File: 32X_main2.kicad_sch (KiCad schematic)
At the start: 54 parts, among them IC501 SH2 M, IC502 SH2 S, IC503 µPD4502161, IC504 315-5818, IC506 315-5781, IC507 TC511664, IC508 TC511664, IC509 74AC04, IC510 RHSRL33A

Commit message: more component parts updated
Full in the * as PAL versions.
Added MPN for PCBWAY
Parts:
- C5, C513, C516, C518, C519, C521, C522, C528, C531, C532, C533, C535, C536, C538, C539, C540, C541, C548: MPN (none) -> VJ0805Y104JXJMT
- C511, C514: MPN (none) -> VJ0805A471FXJPW1BC
- C512, C515, C517, C520, C523, C527, C530, C534, C537, C699: MPN (none) -> VJ1206V475MXJTW1BC
- C525: MPN (none) -> VJ0805A680FXJCW1BC
- C526, C696, C697: MPN (none) -> VJ0805A101FXJPW1BC
- IC509: MPN (none) -> SN74AC04DR
- L501: MPN (none) -> CMI322513J101KT
- R502: MPN (none) -> CRCW080510K0FKEA
- R503, R505: MPN (none) -> CRCW08053K00FKEA
- R506: MPN (none) -> CRCW0805180RJNEA
- R507: MPN (none) -> CRCW080513K0FKEA
- R508: MPN (none) -> CRCW08052K70FKEA
- R509: MPN (none) -> CRCW08051K60FKEA

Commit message: part updates
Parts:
- C525: LCSC Part # C3842272 -> C162306; MPN VJ0805A680FXJCW1BC -> GRM21A5C2J680JWA1D
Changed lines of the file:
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@@
       (effects (font (size 1.27 1.27)) hide)
     )
-    (property "LCSC Part #" "C3842272" (at 215.265 203.835 0)
+    (property "LCSC Part #" "C162306" (at 215.265 203.835 0)
       (effects (font (size 1.27 1.27)) hide)
     )
-    (property "MPN" "VJ0805A680FXJCW1BC" (at 215.265 203.835 0)
+    (property "MPN" "GRM21A5C2J680JWA1D" (at 215.265 203.835 0)
       (effects (font (size 1.27 1.27)) hide)
     )

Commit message: Allow for both wide and narrow IC509.
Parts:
- IC509: footprint Package_SO:SO-14_5.3x10.2mm_P1.27mm -> Neptune:SO-14_Dual_Purpose_P1.27mm
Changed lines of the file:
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@@
       (effects (font (size 1.27 1.27)))
     )
-    (property "Footprint" "Package_SO:SO-14_5.3x10.2mm_P1.27mm" (at 377.19 232.41 0)
+    (property "Footprint" "Neptune:SO-14_Dual_Purpose_P1.27mm" (at 377.19 232.41 0)
       (effects (font (size 1.27 1.27)) hide)
     )
@@
       (effects (font (size 1.27 1.27)))
     )
-    (property "Footprint" "Package_SO:SO-14_5.3x10.2mm_P1.27mm" (at 340.995 232.41 0)
-      (effects (font (size 1.27 1.27)) hide)
-    )
+    (property "Footprint" "Neptune:SO-14_Dual_Purpose_P1.27mm" (at 340.995 232.41 0)
+      (effects (font (size 1.27 1.27)) hide)
+    )

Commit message: Update LCSC parts
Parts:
- C5, C513, C516, C518, C519, C521, C522, C528, C531, C532, C533, C535, C536, C538, C539, C540, C541, C548: LCSC Part # C2237864 -> C111492
- C511, C514: LCSC Part # C2232577 -> C62771
- C512, C515, C517, C520, C523, C527, C530, C534, C537, C699: LCSC Part # C2182015 -> C132170
- C526: LCSC Part # C2232364 -> C62768
- C696, C697: LCSC Part # C2232364 -> C1854109
- R503, R505: LCSC Part # C844841 -> C114222
- R506: LCSC Part # C2077041 -> C137585
- R509: LCSC Part # C2077359 -> C185279
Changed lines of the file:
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@@
       (effects (font (size 1.27 1.27)) hide)
     )
-    (property "LCSC Part #" "C2237864" (at 380.365 55.245 0)
+    (property "LCSC Part #" "C111492" (at 380.365 55.245 0)
       (effects (font (size 1.27 1.27)) hide)
     )
@@
       (effects (font (size 1.27 1.27)) hide)
     )
-    (property "LCSC Part #" "C2182015" (at 367.665 55.245 0)
+    (property "LCSC Part #" "C132170" (at 367.665 55.245 0)
       (effects (font (size 1.27 1.27)) hide)
     )
@@
       (effects (font (size 1.27 1.27)) hide)
     )
-    (property "LCSC Part #" "C2232364" (at 29.845 269.24 0)
+    (property "LCSC Part #" "C1854109" (at 29.845 269.24 0)
       (effects (font (size 1.27 1.27)) hide)
     )
@@
       (effects (font (size 1.27 1.27)) hide)
     )
-    (property "LCSC Part #" "C2232577" (at 146.05 182.245 0)
+    (property "LCSC Part #" "C62771" (at 146.05 182.245 0)
       (effects (font (size 1.27 1.27)) hide)
     )
@@
       (effects (font (size 1.27 1.27)) hide)
     )
-    (property "LCSC Part #" "C2237864" (at 311.785 112.395 0)
+    (property "LCSC Part #" "C111492" (at 311.785 112.395 0)
       (effects (font (size 1.27 1.27)) hide)
     )
@@
       (effects (font (size 1.27 1.27)) hide)
     )
-    (property "LCSC Part #" "C2237864" (at 325.12 112.395 0)
+    (property "LCSC Part #" "C111492" (at 325.12 112.395 0)
       (effects (font (size 1.27 1.27)) hide)
     )
@@
       (effects (font (size 1.27 1.27)) hide)
     )
-    (property "LCSC Part #" "C2237864" (at 393.065 80.01 0)
+    (property "LCSC Part #" "C111492" (at 393.065 80.01 0)
       (effects (font (size 1.27 1.27)) hide)
     )
@@
       (effects (font (size 1.27 1.27)) hide)
     )
-    (property "LCSC Part #" "C2237864" (at 382.27 123.19 0)
+    (property "LCSC Part #" "C111492" (at 382.27 123.19 0)
       (effects (font (size 1.27 1.27)) hide)
     )
@@
       (effects (font (size 1.27 1.27)) hide)
     )
-    (property "LCSC Part #" "C2237864" (at 393.065 123.19 0)
+    (property "LCSC Part #" "C111492" (at 393.065 123.19 0)
       (effects (font (size 1.27 1.27)) hide)
     )
@@
       (effects (font (size 1.27 1.27)) hide)
     )
-    (property "LCSC Part #" "C2237864" (at 370.205 123.19 0)
+    (property "LCSC Part #" "C111492" (at 370.205 123.19 0)
       (effects (font (size 1.27 1.27)) hide)
     )
@@
       (effects (font (size 1.27 1.27)) hide)
     )
-    (property "LCSC Part #" "C2182015" (at 367.665 80.01 0)
+    (property "LCSC Part #" "C132170" (at 367.665 80.01 0)
       (effects (font (size 1.27 1.27)) hide)
     )
@@
       (effects (font (size 1.27 1.27)) hide)
     )
-    (property "LCSC Part #" "C2182015" (at 225.425 75.565 0)
+    (property "LCSC Part #" "C132170" (at 225.425 75.565 0)
       (effects (font (size 1.27 1.27)) hide)
     )
@@
       (effects (font (size 1.27 1.27)) hide)
     )
-    (property "LCSC Part #" "C2237864" (at 358.775 123.19 0)
+    (property "LCSC Part #" "C111492" (at 358.775 123.19 0)
       (effects (font (size 1.27 1.27)) hide)
     )
@@
       (effects (font (size 1.27 1.27)) hide)
     )
-    (property "LCSC Part #" "C2237864" (at 219.71 118.11 0)
+    (property "LCSC Part #" "C111492" (at 219.71 118.11 0)
       (effects (font (size 1.27 1.27)) hide)
     )
@@
       (effects (font (size 1.27 1.27)) hide)
     )
-    (property "LCSC Part #" "C2237864" (at 67.31 192.405 0)
+    (property "LCSC Part #" "C111492" (at 67.31 192.405 0)
       (effects (font (size 1.27 1.27)) hide)
     )
@@
       (effects (font (size 1.27 1.27)) hide)
     )
-    (property "LCSC Part #" "C2237864" (at 137.795 192.405 0)
+    (property "LCSC Part #" "C111492" (at 137.795 192.405 0)
       (effects (font (size 1.27 1.27)) hide)
     )
@@
       (effects (font (size 1.27 1.27)) hide)
     )
-    (property "LCSC Part #" "C2182015" (at 297.815 207.01 0)
+    (property "LCSC Part #" "C132170" (at 297.815 207.01 0)
       (effects (font (size 1.27 1.27)) hide)
     )
@@
       (effects (font (size 1.27 1.27)) hide)
     )
-    (property "LCSC Part #" "C2182015" (at 297.815 112.395 0)
+    (property "LCSC Part #" "C132170" (at 297.815 112.395 0)
       (effects (font (size 1.27 1.27)) hide)
     )
@@
       (effects (font (size 1.27 1.27)) hide)
     )
-    (property "LCSC Part #" "C2237864" (at 273.05 255.27 0)
+    (property "LCSC Part #" "C111492" (at 273.05 255.27 0)
       (effects (font (size 1.27 1.27)) hide)
     )
@@
       (effects (font (size 1.27 1.27)) hide)
     )
-    (property "LCSC Part #" "C2237864" (at 311.785 207.01 0)
+    (property "LCSC Part #" "C111492" (at 311.785 207.01 0)
       (effects (font (size 1.27 1.27)) hide)
     )
@@
       (effects (font (size 1.27 1.27)) hide)
     )
-    (property "LCSC Part #" "C2077359" (at 279.4 255.27 0)
+    (property "LCSC Part #" "C185279" (at 279.4 255.27 0)
       (effects (font (size 1.27 1.27)) hide)
     )
@@
       (effects (font (size 1.27 1.27)) hide)
     )
-    (property "LCSC Part #" "C2237864" (at 294.005 255.27 0)
+    (property "LCSC Part #" "C111492" (at 294.005 255.27 0)
       (effects (font (size 1.27 1.27)) hide)
     )
@@
       (effects (font (size 1.27 1.27)) hide)
     )
-    (property "LCSC Part #" "C2077041" (at 355.6 232.41 0)
+    (property "LCSC Part #" "C137585" (at 355.6 232.41 0)
       (effects (font (size 1.27 1.27)) hide)
     )
@@
       (effects (font (size 1.27 1.27)) hide)
     )
-    (property "LCSC Part #" "C2237864" (at 206.375 118.11 0)
+    (property "LCSC Part #" "C111492" (at 206.375 118.11 0)
       (effects (font (size 1.27 1.27)) hide)
     )
@@
       (effects (font (size 1.27 1.27)) hide)
     )
-    (property "LCSC Part #" "C2232364" (at 46.99 269.24 0)
+    (property "LCSC Part #" "C1854109" (at 46.99 269.24 0)
       (effects (font (size 1.27 1.27)) hide)
     )
@@
       (effects (font (size 1.27 1.27)) hide)
     )
-    (property "LCSC Part #" "C2182015" (at 153.67 192.405 0)
+    (property "LCSC Part #" "C132170" (at 153.67 192.405 0)
       (effects (font (size 1.27 1.27)) hide)
     )
@@
       (effects (font (size 1.27 1.27)) hide)
     )
-    (property "LCSC Part #" "C2237864" (at 236.22 254 0)
+    (property "LCSC Part #" "C111492" (at 236.22 254 0)
       (effects (font (size 1.27 1.27)) hide)
     )
@@
       (effects (font (size 1.27 1.27)) hide)
     )
-    (property "LCSC Part #" "C2182015" (at 83.185 192.405 0)
+    (property "LCSC Part #" "C132170" (at 83.185 192.405 0)
       (effects (font (size 1.27 1.27)) hide)
     )
@@
       (effects (font (size 1.27 1.27)) hide)
     )
-    (property "LCSC Part #" "C2232364" (at 363.855 238.76 0)
+    (property "LCSC Part #" "C62768" (at 363.855 238.76 0)
       (effects (font (size 1.27 1.27)) hide)
     )
@@
       (effects (font (size 1.27 1.27)) hide)
     )
-    (property "LCSC Part #" "C2182015" (at 172.085 94.615 0)
+    (property "LCSC Part #" "C132170" (at 172.085 94.615 0)
       (effects (font (size 1.27 1.27)) hide)
     )
@@
       (effects (font (size 1.27 1.27)) hide)
     )
-    (property "LCSC Part #" "C2237864" (at 393.065 55.245 0)
+    (property "LCSC Part #" "C111492" (at 393.065 55.245 0)
       (effects (font (size 1.27 1.27)) hide)
     )
@@
       (effects (font (size 1.27 1.27)) hide)
     )
-    (property "LCSC Part #" "C2182015" (at 192.405 118.11 0)
+    (property "LCSC Part #" "C132170" (at 192.405 118.11 0)
       (effects (font (size 1.27 1.27)) hide)
     )
@@
       (effects (font (size 1.27 1.27)) hide)
     )
-    (property "LCSC Part #" "C2237864" (at 325.12 207.01 0)
+    (property "LCSC Part #" "C111492" (at 325.12 207.01 0)
       (effects (font (size 1.27 1.27)) hide)
     )
@@
       (effects (font (size 1.27 1.27)) hide)
     )
-    (property "LCSC Part #" "C2237864" (at 380.365 80.01 0)
+    (property "LCSC Part #" "C111492" (at 380.365 80.01 0)
       (effects (font (size 1.27 1.27)) hide)
     )
@@
       (effects (font (size 1.27 1.27)) hide)
     )
-    (property "LCSC Part #" "C844841" (at 69.85 177.165 0)
+    (property "LCSC Part #" "C114222" (at 69.85 177.165 0)
       (effects (font (size 1.27 1.27)) hide)
     )
@@
       (effects (font (size 1.27 1.27)) hide)
     )
-    (property "LCSC Part #" "C844841" (at 140.335 177.165 0)
+    (property "LCSC Part #" "C114222" (at 140.335 177.165 0)
       (effects (font (size 1.27 1.27)) hide)
     )
@@
       (effects (font (size 1.27 1.27)) hide)
     )
-    (property "LCSC Part #" "C2237864" (at 231.14 75.565 0)
+    (property "LCSC Part #" "C111492" (at 231.14 75.565 0)
       (effects (font (size 1.27 1.27)) hide)
     )
@@
       (effects (font (size 1.27 1.27)) hide)
     )
-    (property "LCSC Part #" "C2182015" (at 223.52 254 0)
+    (property "LCSC Part #" "C132170" (at 223.52 254 0)
       (effects (font (size 1.27 1.27)) hide)
     )
@@
       (effects (font (size 1.27 1.27)) hide)
     )
-    (property "LCSC Part #" "C2237864" (at 236.855 75.565 0)
+    (property "LCSC Part #" "C111492" (at 236.855 75.565 0)
       (effects (font (size 1.27 1.27)) hide)
     )
@@
       (effects (font (size 1.27 1.27)) hide)
     )
-    (property "LCSC Part #" "C2232577" (at 75.565 182.245 0)
+    (property "LCSC Part #" "C62771" (at 75.565 182.245 0)
       (effects (font (size 1.27 1.27)) hide)
     )

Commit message: BOM tweaks.
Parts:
- C526: value 100/120pF -> 100/120pF (VA1/VA0)
- C696, C697: value 100pF -> Unused/47/100pF
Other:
- note removed: "VA1/VA0"
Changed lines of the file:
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@@
     (title "32X Main 2")
     (date "2023-11-29")
-    (rev "1.1b")
+    (rev "1.2a")
     (company "By Cosam")
     (comment 1 "Neptune")
@@
     (effects (font (size 1.27 1.27)) (justify left bottom))
   )
-  (text "VA1/VA0" (at 350.52 243.205 0)
-    (effects (font (size 1.27 1.27)) (justify left bottom))
-  )
   (text "Originally C96 and C97, which are THT capacitors\nsoldered directly to the chips on VA1 main boards.\nRenumbered 6xx to replace with SMD parts."
     (at 57.15 280.67 0)
@@
       (effects (font (size 1.27 1.27)) (justify right))
     )
-    (property "Value" "100pF" (at 26.67 270.51 0)
+    (property "Value" "Unused/47/100pF" (at 26.67 270.51 0)
       (effects (font (size 1.27 1.27)) (justify right) hide)
     )
@@
   (symbol (lib_id "74xx:74LS04") (at 377.19 232.41 0) (unit 6)
     (in_bom yes) (on_board yes) (dnp no)
-    (property "Reference" "IC509" (at 377.19 238.76 0)
+    (property "Reference" "IC509" (at 377.19 223.52 0)
       (effects (font (size 1.27 1.27)))
     )
-    (property "Value" "74AC04" (at 377.19 241.3 0)
+    (property "Value" "74AC04" (at 377.19 226.06 0)
       (effects (font (size 1.27 1.27)))
     )
@@
       (effects (font (size 1.27 1.27)) (justify right))
     )
-    (property "Value" "100pF" (at 43.815 270.51 0)
+    (property "Value" "Unused/47/100pF" (at 43.815 270.51 0)
       (effects (font (size 1.27 1.27)) (justify right) hide)
     )
@@
   (symbol (lib_id "Device:C") (at 363.855 238.76 0) (unit 1)
     (in_bom yes) (on_board yes) (dnp no)
-    (property "Reference" "C526" (at 360.68 237.49 0)
+    (property "Reference" "C526" (at 372.745 240.665 0)
       (effects (font (size 1.27 1.27)) (justify right))
     )
-    (property "Value" "100/120pF" (at 360.68 240.03 0)
+    (property "Value" "100/120pF (VA1/VA0)" (at 389.255 243.205 0)
       (effects (font (size 1.27 1.27)) (justify right))
     )
@@
   (symbol (lib_id "74xx:74LS04") (at 340.995 232.41 0) (unit 2)
     (in_bom yes) (on_board yes) (dnp no)
-    (property "Reference" "IC509" (at 340.995 238.76 0)
+    (property "Reference" "IC509" (at 340.995 223.52 0)
       (effects (font (size 1.27 1.27)))
     )
-    (property "Value" "74AC04" (at 340.995 241.3 0)
+    (property "Value" "74AC04" (at 340.995 226.06 0)
       (effects (font (size 1.27 1.27)))
     )

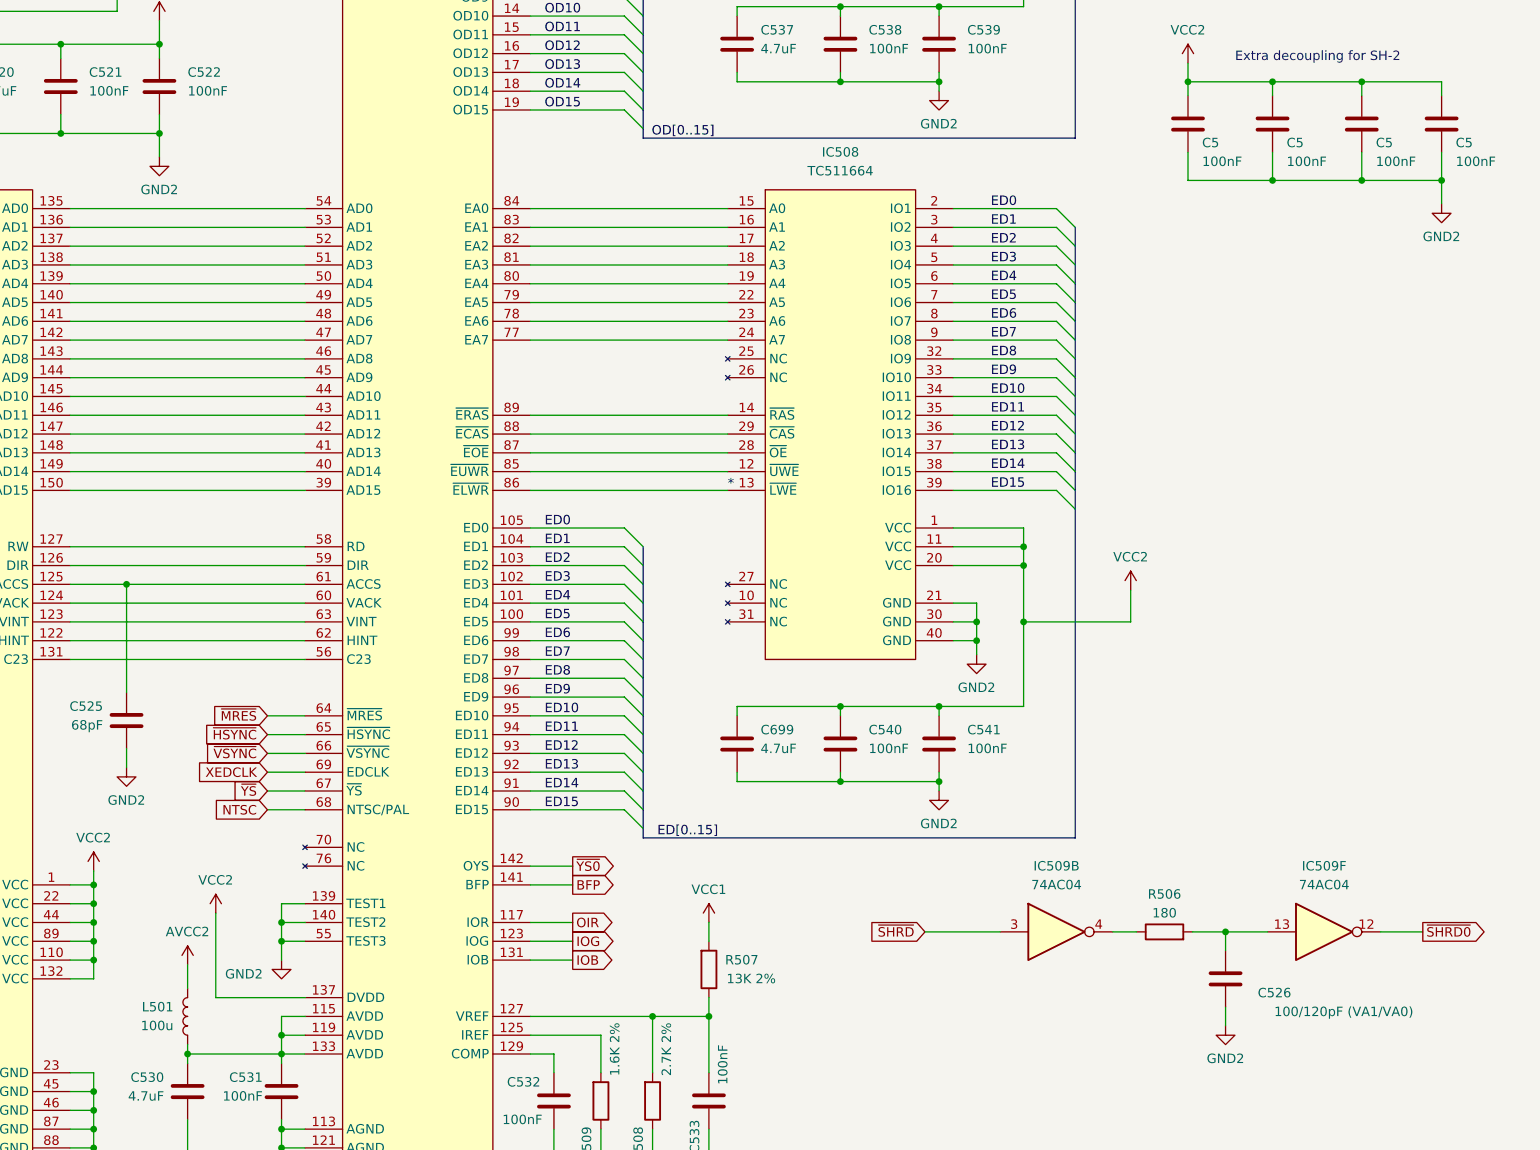
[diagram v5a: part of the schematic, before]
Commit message: MRES diode fix, use more common BGKR LED pinout and larger footprint.
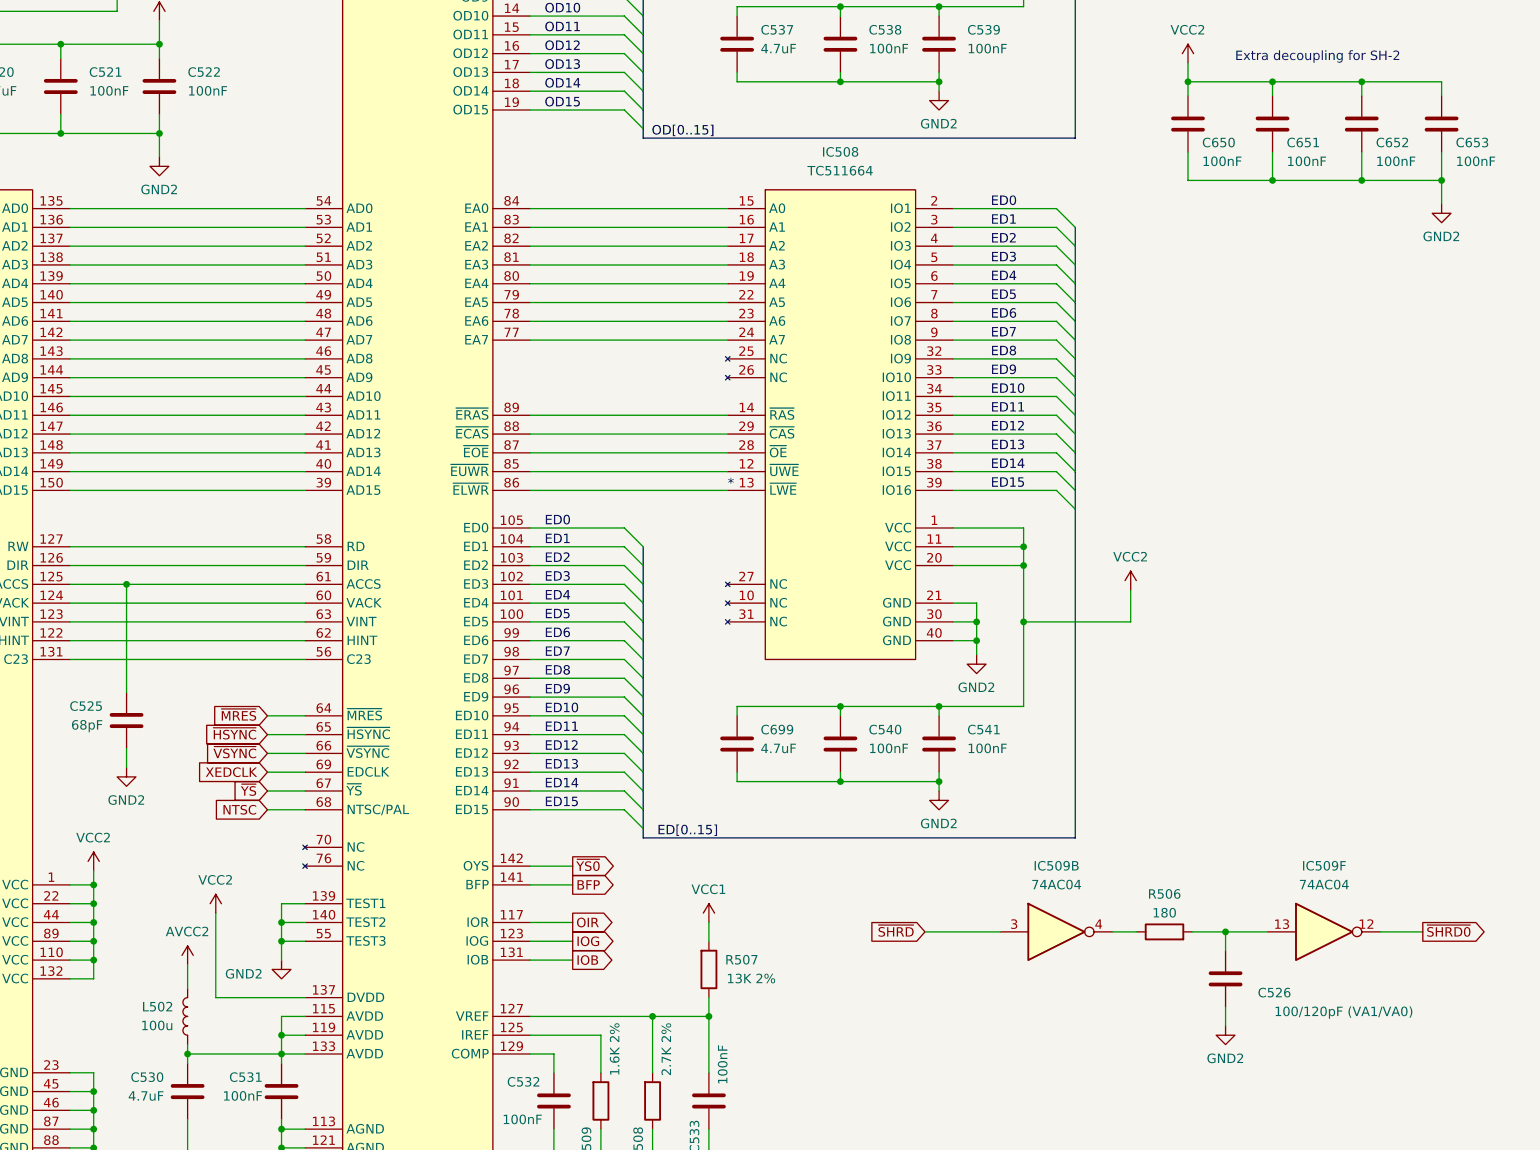
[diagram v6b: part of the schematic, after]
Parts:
- renumbered C5 to C650, C5 to C651, C5 to C652, C5 to C653, L501 to L502
